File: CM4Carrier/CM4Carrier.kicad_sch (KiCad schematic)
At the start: 2 parts

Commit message: symb.
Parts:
- added U?: MAX2723, symbol CM4IO:MAX2723
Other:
- note added: "max2723A 3A"
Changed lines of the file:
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@@
 (kicad_sch (version 20211123) (generator eeschema)
   (paper "A4")
+  (text "max2723A 3A \n" (at 153.035 71.12 0)
+    (effects (font (size 1.27 1.27)) (justify left bottom))
+  )
+  (symbol (lib_id "CM4IO:MAX2723") (at 161.29 118.745 0) (unit 1)
+    (in_bom yes) (on_board yes) (fields_autoplaced)
+    (property "Reference" "U?" (id 0) (at 161.925 92.71 0))
+    (property "Value" "MAX2723" (id 1) (at 161.925 95.25 0))
+    (property "Footprint" "" (id 2) (at 161.29 118.745 0)
+      (effects (font (size 1.27 1.27)) hide)
+    )
+    (property "Datasheet" "https://www.mouser.co.uk/datasheet/2/277/MP2723AGQC-2900665.pdf" (id 3) (at 161.29 118.745 0)
+      (effects (font (size 1.27 1.27)) hide)
+    )
+    (pin "1")
+    (pin "10")
+    (pin "11")
+    (pin "12")
+    (pin "13")
+    (pin "14")
+    (pin "15")
+    (pin "16")
+    (pin "17")
+    (pin "18")
+    (pin "19")
+    (pin "2")
+    (pin "20")
+    (pin "21")
+    (pin "22")
+    (pin "23")
+    (pin "24")
+    (pin "25")
+    (pin "26")
+    (pin "3")
+    (pin "4")
+    (pin "5")
+    (pin "6")
+    (pin "7")
+    (pin "8")
+    (pin "9")
+  )
   (symbol (lib_id "CM4IO:ComputeModule4-CM4") (at 26.035 33.02 0) (unit 1)
     (in_bom yes) (on_board yes) (fields_autoplaced)
@@
       (reference "Module?") (unit 2) (value "ComputeModule4-CM4") (footprint "CM4IO:Raspberry-Pi-4-Compute-Module")
     )
-  )
+    (path "/e4f105bc-211e-404e-b603-9e46f15797b0"
+      (reference "U?") (unit 1) (value "MAX2723") (footprint "")
+    )
+  )

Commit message: h
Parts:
- removed Module? (x2): ComputeModule4-CM4, CM4IO:Raspberry-Pi-4-Compute-Module, symbol CM4IO:ComputeModule4-CM4
- removed U?: MAX2723, symbol CM4IO:MAX2723
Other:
- added sheet IO (heiarchy\io.kicad.kicad_sch)
- note removed: "max2723A 3A"

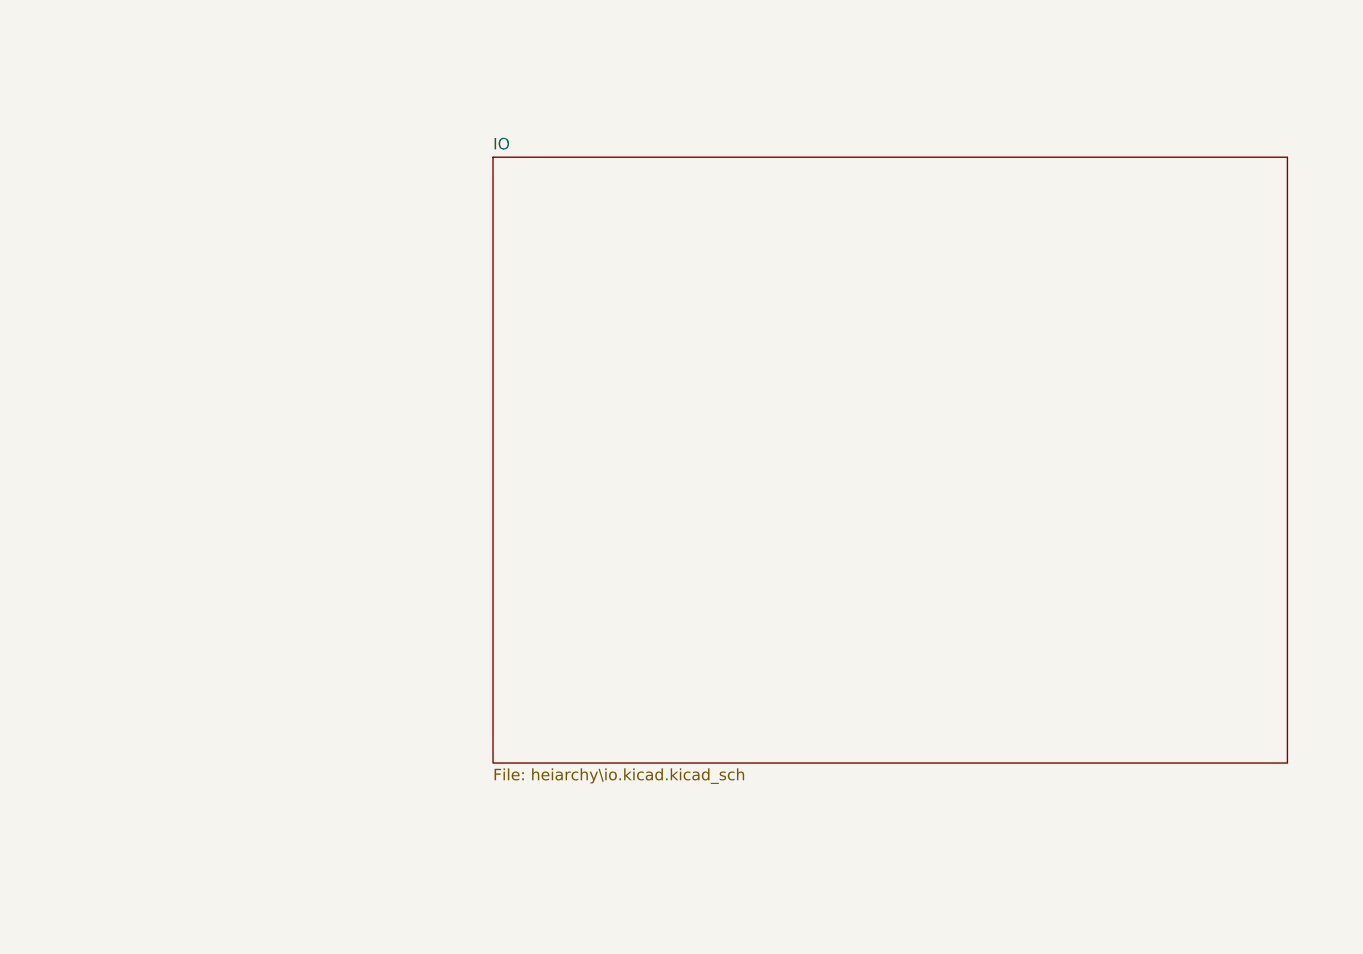
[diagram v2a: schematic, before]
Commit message: Adaptor board
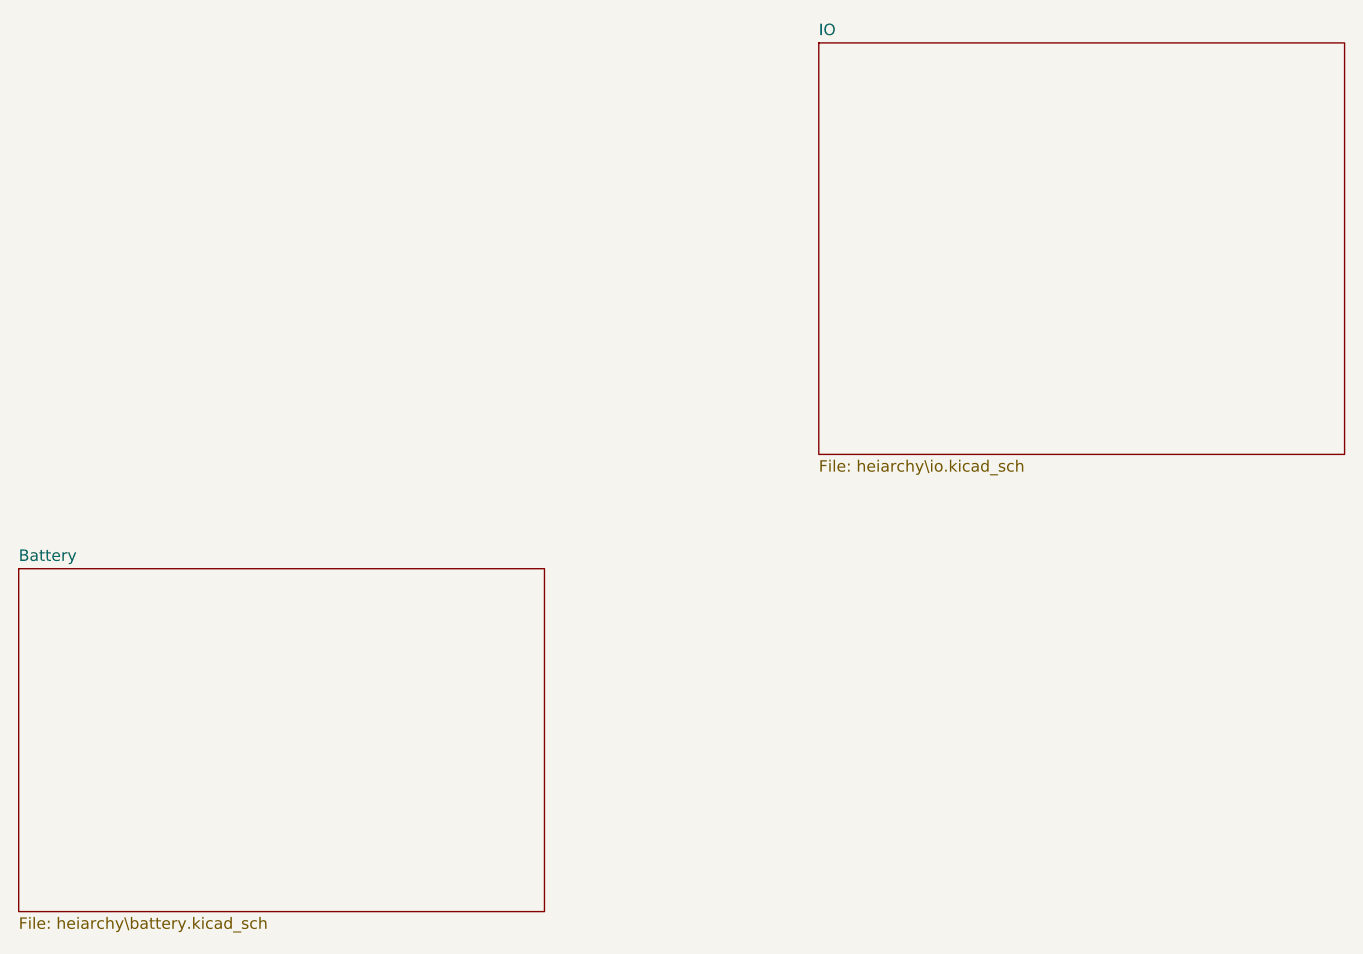
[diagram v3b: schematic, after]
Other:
- added sheet Battery (heiarchy\battery.kicad_sch)
- sheet IO: file heiarchy\io.kicad.kicad_sch -> heiarchy\io.kicad_sch
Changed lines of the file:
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@@
 (kicad_sch (version 20211123) (generator eeschema)
   (paper "A4")
-  (sheet (at 149.225 66.04) (size 88.265 67.31) (fields_autoplaced)
+  (sheet (at 185.42 53.34) (size 58.42 45.72) (fields_autoplaced)
     (stroke (width 0.1524) (type solid) (color 0 0 0 0))
     (fill (color 0 0 0 0.0000))
-    (property "Sheet name" "IO" (id 0) (at 149.225 65.3284 0)
+    (property "Sheet name" "IO" (id 0) (at 185.42 52.6284 0)
       (effects (font (size 1.27 1.27)) (justify left bottom))
     )
-    (property "Sheet file" "heiarchy\\io.kicad.kicad_sch" (id 1) (at 149.225 133.9346 0)
+    (property "Sheet file" "heiarchy\\io.kicad_sch" (id 1) (at 185.42 99.6446 0)
+      (effects (font (size 1.27 1.27)) (justify left top))
+    )
+  )
+  (sheet (at 96.52 111.76) (size 58.42 38.1) (fields_autoplaced)
+    (stroke (width 0.1524) (type solid) (color 0 0 0 0))
+    (fill (color 0 0 0 0.0000))
+    (property "Sheet name" "Battery" (id 0) (at 96.52 111.0484 0)
+      (effects (font (size 1.27 1.27)) (justify left bottom))
+    )
+    (property "Sheet file" "heiarchy\\battery.kicad_sch" (id 1) (at 96.52 150.4446 0)
       (effects (font (size 1.27 1.27)) (justify left top))
     )
@@
     (path "/" (page "1"))
     (path "/1d948cd0-f6e4-4bae-aaaf-c0cfc5cdd7a9" (page "2"))
+    (path "/a75f8253-7851-4062-bd61-8fb400fa95f7" (page "3"))
   )
   (symbol_instances
@@
       (reference "Module?") (unit 2) (value "ComputeModule4-CM4") (footprint "CM4IO:Raspberry-Pi-4-Compute-Module")
     )
+    (path "/a75f8253-7851-4062-bd61-8fb400fa95f7/2a3e3937-f1c9-4371-a1ef-6f37a588e608"
+      (reference "U?") (unit 1) (value "MAX77751") (footprint "")
+    )
   )

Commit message: aa
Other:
- added sheet Buttons (heiarchy\buttons.kicad_sch)
- sheet Battery ports: added CHRG-CC1, CHRG-CC2, CHRG-D+, CHRG-D-, CHRG-VBUS, _5v; removed none
- sheet IO ports: added _5v; removed none
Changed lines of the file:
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@@
 (kicad_sch (version 20211123) (generator eeschema)
   (paper "A4")
-  (sheet (at 185.42 53.34) (size 58.42 45.72) (fields_autoplaced)
+  (wire (pts (xy 193.04 121.92) (xy 199.39 121.92))
+    (stroke (width 0) (type default) (color 0 0 0 0))
+  )
+  (label "_5v" (at 194.31 121.92 0)
+    (effects (font (size 1.27 1.27)) (justify left bottom))
+  )
+  (sheet (at 199.39 85.09) (size 58.42 38.1) (fields_autoplaced)
     (stroke (width 0.1524) (type solid) (color 0 0 0 0))
     (fill (color 0 0 0 0.0000))
-    (property "Sheet name" "IO" (id 0) (at 185.42 52.6284 0)
+    (property "Sheet name" "IO" (id 0) (at 199.39 84.3784 0)
       (effects (font (size 1.27 1.27)) (justify left bottom))
     )
-    (property "Sheet file" "heiarchy\\io.kicad_sch" (id 1) (at 185.42 99.6446 0)
+    (property "Sheet file" "heiarchy\\io.kicad_sch" (id 1) (at 199.39 123.7746 0)
       (effects (font (size 1.27 1.27)) (justify left top))
     )
+    (pin "_5v" input (at 199.39 121.92 180)
+      (effects (font (size 1.27 1.27)) (justify left))
+    )
   )
-  (sheet (at 96.52 111.76) (size 58.42 38.1) (fields_autoplaced)
+  (sheet (at 134.62 85.09) (size 58.42 38.1) (fields_autoplaced)
     (stroke (width 0.1524) (type solid) (color 0 0 0 0))
     (fill (color 0 0 0 0.0000))
-    (property "Sheet name" "Battery" (id 0) (at 96.52 111.0484 0)
+    (property "Sheet name" "Battery" (id 0) (at 134.62 84.3784 0)
       (effects (font (size 1.27 1.27)) (justify left bottom))
     )
-    (property "Sheet file" "heiarchy\\battery.kicad_sch" (id 1) (at 96.52 150.4446 0)
+    (property "Sheet file" "heiarchy\\battery.kicad_sch" (id 1) (at 134.62 123.7746 0)
+      (effects (font (size 1.27 1.27)) (justify left top))
+    )
+    (pin "CHRG-D-" bidirectional (at 193.04 87.63 0)
+      (effects (font (size 1.27 1.27)) (justify right))
+    )
+    (pin "CHRG-D+" bidirectional (at 193.04 90.17 0)
+      (effects (font (size 1.27 1.27)) (justify right))
+    )
+    (pin "CHRG-CC1" bidirectional (at 193.04 92.71 0)
+      (effects (font (size 1.27 1.27)) (justify right))
+    )
+    (pin "CHRG-CC2" bidirectional (at 193.04 95.25 0)
+      (effects (font (size 1.27 1.27)) (justify right))
+    )
+    (pin "CHRG-VBUS" input (at 193.04 97.79 0)
+      (effects (font (size 1.27 1.27)) (justify right))
+    )
+    (pin "_5v" output (at 193.04 121.92 0)
+      (effects (font (size 1.27 1.27)) (justify right))
+    )
+  )
+  (sheet (at 26.67 54.61) (size 66.04 27.94) (fields_autoplaced)
+    (stroke (width 0.1524) (type solid) (color 0 0 0 0))
+    (fill (color 0 0 0 0.0000))
+    (property "Sheet name" "Buttons" (id 0) (at 26.67 53.8984 0)
+      (effects (font (size 1.27 1.27)) (justify left bottom))
+    )
+    (property "Sheet file" "heiarchy\\buttons.kicad_sch" (id 1) (at 26.67 83.1346 0)
       (effects (font (size 1.27 1.27)) (justify left top))
     )
@@
     (path "/1d948cd0-f6e4-4bae-aaaf-c0cfc5cdd7a9" (page "2"))
     (path "/a75f8253-7851-4062-bd61-8fb400fa95f7" (page "3"))
+    (path "/fbd4ebba-c181-4efc-9928-2457cd7bdbdb" (page "4"))
   )
   (symbol_instances
+    (path "/fbd4ebba-c181-4efc-9928-2457cd7bdbdb/512b3433-27dd-4461-a82b-3f1d2f9d0032"
+      (reference "#PWR?") (unit 1) (value "GND") (footprint "")
+    )
+    (path "/a75f8253-7851-4062-bd61-8fb400fa95f7/75214b83-389e-4513-b3a1-83ea320bfdc3"
+      (reference "#PWR?") (unit 1) (value "GNDPWR") (footprint "")
+    )
+    (path "/1d948cd0-f6e4-4bae-aaaf-c0cfc5cdd7a9/975738a4-9d90-4b57-895c-9ecfdda01dbe"
+      (reference "#PWR?") (unit 1) (value "GND") (footprint "")
+    )
+    (path "/1d948cd0-f6e4-4bae-aaaf-c0cfc5cdd7a9/bafeaaaa-53db-4cac-b7cf-74df06675a4c"
+      (reference "#PWR?") (unit 1) (value "GND") (footprint "")
+    )
+    (path "/fbd4ebba-c181-4efc-9928-2457cd7bdbdb/cb8af5b5-e158-402c-9929-59141c6fdc21"
+      (reference "#PWR?") (unit 1) (value "GND") (footprint "")
+    )
+    (path "/a75f8253-7851-4062-bd61-8fb400fa95f7/e6668668-d1fc-4148-b6ba-63223bb98677"
+      (reference "#PWR?") (unit 1) (value "GND") (footprint "")
+    )
+    (path "/fbd4ebba-c181-4efc-9928-2457cd7bdbdb/231aecb7-7111-4be8-9562-00b437a5b813"
+      (reference "C?") (unit 1) (value "1u") (footprint "")
+    )
+    (path "/fbd4ebba-c181-4efc-9928-2457cd7bdbdb/7d1ad62c-a41b-4fd6-abef-1925c670f70a"
+      (reference "C?") (unit 1) (value "1u") (footprint "")
+    )
     (path "/1d948cd0-f6e4-4bae-aaaf-c0cfc5cdd7a9/f7ad27ec-86fc-436e-b780-930660cc0e1f"
       (reference "Module?") (unit 1) (value "ComputeModule4-CM4") (footprint "CM4IO:Raspberry-Pi-4-Compute-Module")
@@
       (reference "Module?") (unit 2) (value "ComputeModule4-CM4") (footprint "CM4IO:Raspberry-Pi-4-Compute-Module")
     )
+    (path "/fbd4ebba-c181-4efc-9928-2457cd7bdbdb/46d2bf68-6d38-42f7-ae9d-e73d8ce6d0bc"
+      (reference "R?") (unit 1) (value "100k") (footprint "")
+    )
+    (path "/fbd4ebba-c181-4efc-9928-2457cd7bdbdb/c3c90041-45ba-433c-96af-6bad51c3b7cc"
+      (reference "R?") (unit 1) (value "5M") (footprint "")
+    )
+    (path "/fbd4ebba-c181-4efc-9928-2457cd7bdbdb/cb9a70d9-40bd-45e0-a7a6-34cabe020231"
+      (reference "R?") (unit 1) (value "100k") (footprint "")
+    )
+    (path "/fbd4ebba-c181-4efc-9928-2457cd7bdbdb/552ad4e0-2fe1-42ea-b68c-f8a61536fc9c"
+      (reference "SW?") (unit 1) (value "SW_Push") (footprint "")
+    )
     (path "/a75f8253-7851-4062-bd61-8fb400fa95f7/2a3e3937-f1c9-4371-a1ef-6f37a588e608"
       (reference "U?") (unit 1) (value "MAX77751") (footprint "")
     )
+    (path "/fbd4ebba-c181-4efc-9928-2457cd7bdbdb/fd2605d7-a46a-4354-8d8e-3fff3b7fe671"
+      (reference "U?") (unit 1) (value "74HC00") (footprint "")
+    )
+    (path "/fbd4ebba-c181-4efc-9928-2457cd7bdbdb/865384e1-8776-433f-8420-1be45ec75c76"
+      (reference "U?") (unit 2) (value "74HC00") (footprint "")
+    )
+    (path "/fbd4ebba-c181-4efc-9928-2457cd7bdbdb/50b85a3f-d9fc-47eb-adf8-37c96de60746"
+      (reference "U?") (unit 5) (value "74HC00") (footprint "")
+    )
   )

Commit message: aaa
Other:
- sheet Battery ports: added EN; removed none
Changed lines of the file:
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@@
       (effects (font (size 1.27 1.27)) (justify right))
+    )
+    (pin "EN" input (at 134.62 120.65 180)
+      (effects (font (size 1.27 1.27)) (justify left))
     )
   )
@@
       (reference "#PWR011") (unit 1) (value "GND") (footprint "")
     )
+    (path "/a75f8253-7851-4062-bd61-8fb400fa95f7/093e31d6-7a58-400c-8c7e-f6bd356910cd"
+      (reference "#PWR?") (unit 1) (value "GND") (footprint "")
+    )
+    (path "/a75f8253-7851-4062-bd61-8fb400fa95f7/34428195-efd4-44fe-9df4-5ea77be24509"
+      (reference "#PWR?") (unit 1) (value "GND") (footprint "")
+    )
+    (path "/a75f8253-7851-4062-bd61-8fb400fa95f7/658ec26f-ff21-4537-83cf-4e3b8cc4c0e7"
+      (reference "#PWR?") (unit 1) (value "GND") (footprint "")
+    )
+    (path "/a75f8253-7851-4062-bd61-8fb400fa95f7/6cb6ac3f-6fd5-4c85-997b-ad5b83fc594a"
+      (reference "#PWR?") (unit 1) (value "GND") (footprint "")
+    )
+    (path "/a75f8253-7851-4062-bd61-8fb400fa95f7/79e713d8-87f2-4786-8392-39b986766514"
+      (reference "#PWR?") (unit 1) (value "GND") (footprint "")
+    )
+    (path "/a75f8253-7851-4062-bd61-8fb400fa95f7/b56d24b2-597d-4412-a380-f5af22f83cd6"
+      (reference "#PWR?") (unit 1) (value "GND") (footprint "")
+    )
+    (path "/a75f8253-7851-4062-bd61-8fb400fa95f7/bf1cc1d8-4449-45ed-84f4-71ab82e73e70"
+      (reference "#PWR?") (unit 1) (value "GND") (footprint "")
+    )
+    (path "/1d948cd0-f6e4-4bae-aaaf-c0cfc5cdd7a9/f94b5abf-cb2e-4773-93ad-11c3d8c13765"
+      (reference "#PWR?") (unit 1) (value "GND") (footprint "")
+    )
     (path "/a75f8253-7851-4062-bd61-8fb400fa95f7/f9b8bcea-e4ba-4669-b98e-16cee77df8f4"
       (reference "#PWR?") (unit 1) (value "GND") (footprint "")
@@
       (reference "C10") (unit 1) (value "1u") (footprint "")
     )
+    (path "/a75f8253-7851-4062-bd61-8fb400fa95f7/1ad94ddf-e798-437a-8654-59c3e43d4b9a"
+      (reference "C?") (unit 1) (value "C") (footprint "")
+    )
+    (path "/a75f8253-7851-4062-bd61-8fb400fa95f7/536d0e2c-41cf-441c-bd09-a4f2fd08743d"
+      (reference "C?") (unit 1) (value "C") (footprint "")
+    )
+    (path "/a75f8253-7851-4062-bd61-8fb400fa95f7/571086dc-5e71-4768-bd8f-e006212ea1d5"
+      (reference "C?") (unit 1) (value "C") (footprint "")
+    )
+    (path "/a75f8253-7851-4062-bd61-8fb400fa95f7/69032c29-c70f-418a-989b-e12501551f19"
+      (reference "C?") (unit 1) (value "C") (footprint "")
+    )
+    (path "/a75f8253-7851-4062-bd61-8fb400fa95f7/9b9aa4ec-ed68-4ca0-a8fd-0ac5666ecaf9"
+      (reference "C?") (unit 1) (value "C") (footprint "")
+    )
     (path "/a75f8253-7851-4062-bd61-8fb400fa95f7/416d08d8-ffd3-470c-8abb-28df00a38973"
       (reference "D1") (unit 1) (value "LED") (footprint "")
@@
       (reference "D2") (unit 1) (value "LED") (footprint "")
     )
+    (path "/1d948cd0-f6e4-4bae-aaaf-c0cfc5cdd7a9/6010d012-214c-4430-877c-5992786f91c0"
+      (reference "J?") (unit 1) (value "Micro_SD_Card") (footprint "")
+    )
     (path "/a75f8253-7851-4062-bd61-8fb400fa95f7/22500fa5-ec3f-43b8-b073-b8a485720681"
       (reference "L1") (unit 1) (value "1") (footprint "")
     )
+    (path "/a75f8253-7851-4062-bd61-8fb400fa95f7/b2c39ed5-a75e-4531-8b79-22abbd63e22c"
+      (reference "L?") (unit 1) (value "L") (footprint "")
+    )
     (path "/1d948cd0-f6e4-4bae-aaaf-c0cfc5cdd7a9/f7ad27ec-86fc-436e-b780-930660cc0e1f"
       (reference "Module1") (unit 1) (value "ComputeModule4-CM4") (footprint "CM4IO:Raspberry-Pi-4-Compute-Module")
@@
       (reference "R7") (unit 1) (value "100k") (footprint "")
     )
+    (path "/1d948cd0-f6e4-4bae-aaaf-c0cfc5cdd7a9/15b7be2c-eed8-4478-8c69-e13b301c116a"
+      (reference "R?") (unit 1) (value "10M") (footprint "")
+    )
+    (path "/a75f8253-7851-4062-bd61-8fb400fa95f7/2df5cd30-f0f4-4aa0-9225-8bce3cf63f60"
+      (reference "R?") (unit 1) (value "R") (footprint "")
+    )
+    (path "/a75f8253-7851-4062-bd61-8fb400fa95f7/53f61302-578a-42f9-8919-b2b8729908cb"
+      (reference "R?") (unit 1) (value "R") (footprint "")
+    )
+    (path "/a75f8253-7851-4062-bd61-8fb400fa95f7/6a6806ff-bdf1-45ef-8871-321061747ce8"
+      (reference "R?") (unit 1) (value "R") (footprint "")
+    )
+    (path "/a75f8253-7851-4062-bd61-8fb400fa95f7/744d4605-cdec-46dd-b6bc-8c97604a042b"
+      (reference "R?") (unit 1) (value "R") (footprint "")
+    )
+    (path "/a75f8253-7851-4062-bd61-8fb400fa95f7/cd129416-a54b-44b6-9e63-a9c14bfc0a9c"
+      (reference "R?") (unit 1) (value "R") (footprint "")
+    )
     (path "/fbd4ebba-c181-4efc-9928-2457cd7bdbdb/552ad4e0-2fe1-42ea-b68c-f8a61536fc9c"
       (reference "SW1") (unit 1) (value "SW_Push") (footprint "")
@@
       (reference "U2") (unit 5) (value "74HC00") (footprint "")
     )
-  )
+    (path "/a75f8253-7851-4062-bd61-8fb400fa95f7/8ab6bf6d-af54-4c57-8042-2c12cb7a4d0f"
+      (reference "U?") (unit 1) (value "MP3424") (footprint "CM4IO:MP3424GGP")
+    )
+  )

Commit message: Additions
- Fixed gitignore (Backups)
- Work on buttons
- Work on ADC for JOYSTICK
- Work on some other stuff
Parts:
- added C?: (no value), symbol Device:C
- added R? (x2): (no value), symbol Device:R
- added SW?: (no value), symbol Switch:SW_Push
- added TP?: ~, symbol Connector:TestPoint_Flag
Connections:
- new net: R?.1, SW?.2
- new net A: C?.1, R?.2, R?.2, TP?.1
- new net GND: C?.2, SW?.1
- new net GPIO_VOLTAGE: R?.1
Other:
- added sheet IO B (heiarchy/io_b.kicad_sch)
- sheet Battery: file heiarchy\battery.kicad_sch -> heiarchy/battery.kicad_sch
- sheet Buttons: file heiarchy\buttons.kicad_sch -> heiarchy/buttons.kicad_sch
- sheet Buttons ports: added GLOBAL-EN, V_GPIO; removed none
- sheet IO: file heiarchy\io.kicad_sch -> heiarchy/io.kicad_sch
- sheet IO ports: added GLOBAL_EN, IO_VREF; removed none
- note added: "Connections: SD Card Buttons (Power,A,B,X,Y,Start,Sel) Joystick (digital)"
- note added: "Connections: USB 2.0 (A) DSI Connector (Display)"
- note added: "Joystick Buttons: - a - b - x - y - start - sel Power (GLOBAL EN) Power (Boost converter)"

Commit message: wiring some stuff
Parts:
- removed C?: (no value), symbol Device:C
- removed R? (x2): (no value), symbol Device:R
- removed SW?: (no value), symbol Switch:SW_Push
- removed TP?: ~, symbol Connector:TestPoint_Flag
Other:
- sheet Buttons ports: added A, ADC_CS', ADC_MISO, ADC_MOSI, ADC_SCLK, B, DET_SHUTDOWN, DPAD_D, DPAD_L, DPAD_R, DPAD_U, SEL, START, X, Y; removed none
